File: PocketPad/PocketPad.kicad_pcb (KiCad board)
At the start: 2 copper layers, 75 x 65 mm, 45 parts, among them SW0 SW_THT_6x6, SW1 SW_THT_6x6, SW10 SW_THT_6x6, SW11 SW_THT_6x6, SW12 SW_THT_6x6, SW13 SW_THT_6x6, SW14 SW_THT_6x6, SW15 SW_THT_6x6, SW16 SW_THT_6x6, SW17 SW_THT_6x6, SW2 SW_THT_6x6, SW3 SW_THT_6x6, SW4 SW_THT_6x6, SW5 SW_THT_6x6, SW6 SW_THT_6x6, SW7 SW_THT_6x6, SW8 SW_THT_6x6, SW9 SW_THT_6x6

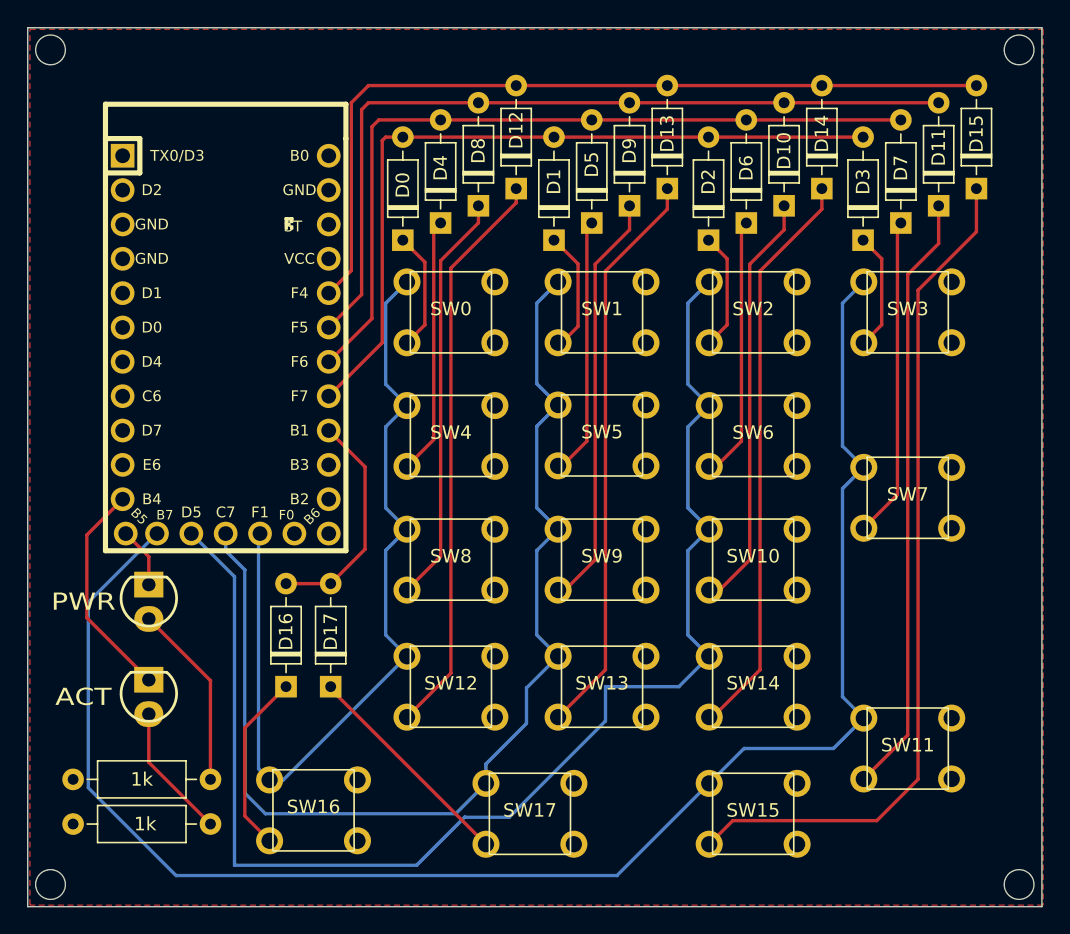
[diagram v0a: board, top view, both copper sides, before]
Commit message: Adjusted placement of switches and trace routes
Overall size reduced
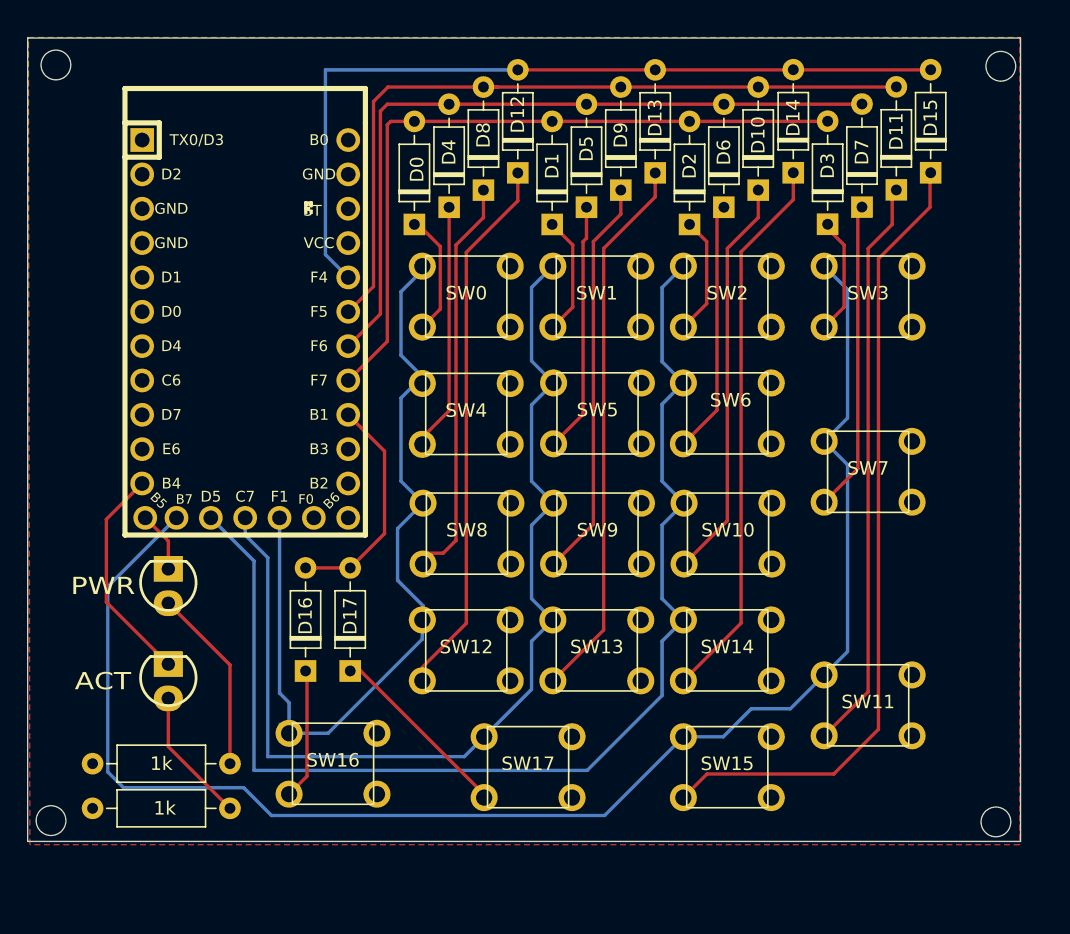
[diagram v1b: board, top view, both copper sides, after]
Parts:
- moved REF** 4.94 mm to (93.6, 75.3)
- moved REF** 4.73 mm to (23.8, 75.2)
- moved SW11 4.33 mm to (84.2, 66.9)
- moved SW15 3.94 mm to (73.8, 71.5)
- moved SW16 3.74 mm to (44.6, 71.2)
- moved D15 3.58 mm to (88.8, 27.3)
- moved SW7 3.50 mm to (84.2, 49.6)
- moved SW17 3.45 mm to (59.0, 71.5)
- moved D11 3.34 mm to (86.3, 28.5)
- moved SW14 3.30 mm to (73.8, 62.8)
- moved SW3 3.15 mm to (84.2, 36.7)
- moved D7 3.11 mm to (83.7, 29.8)
- moved SW12 2.92 mm to (54.5, 62.8)
- moved D3 2.87 mm to (81.2, 31.1)
- moved SW13 2.71 mm to (64.1, 62.8)
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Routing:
- net COL2: track 100.4 -> 88.8 mm
- net COL3: track 120.6 -> 112.6 mm
- net COL1: track 82.4 -> 75.9 mm
- net ROW2: track 60.0 -> 55.7 mm
- net Net-(SW16-Pad3): track 13.4 -> 9.71 mm
- net Net-(SW15-Pad3): track 62.9 -> 59.4 mm
- net ROW1: track 58.0 -> 54.5 mm
- net ROW0: track 56.2 -> 52.8 mm
- net Net-(SW12-Pad3): track 42.4 -> 39.5 mm
- net Net-(SW17-Pad3): track 16.4 -> 14.1 mm
- net Net-(SW11-Pad3): track 44.7 -> 42.4 mm
- net Net-(SW13-Pad3): track 42.4 -> 40.7 mm
- net COL0: track 64.2 -> 62.8 mm
- net Net-(SW14-Pad3): track 42.4 -> 41.2 mm
- net Net-(SW8-Pad3): track 30.6 -> 29.6 mm
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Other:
- board size 75 x 65 mm -> 73.4 x 59.4 mm

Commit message: uploaded latest save
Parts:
- moved PWR-R1 0.58 mm to (27.4, 71.1)
- moved ACT-R1 0.55 mm to (37.5, 74.3)
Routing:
- net COL3: track 112.6 -> 109.8 mm
- net COL0: track 62.8 -> 61.6 mm
- net Net-(ACT-R1-Pad1): track 10.0 -> 11.0 mm
- net COL2: track 88.8 -> 88.0 mm
